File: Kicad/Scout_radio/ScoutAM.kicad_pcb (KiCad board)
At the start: 2 copper layers, 55 x 100 mm, 92 parts, among them J1 Conn_01x07, J2 Conn_01x02, J3 PJ-342, J4 Conn_Coaxial, J5 Conn_01x02, Q1 AO3401A, Q2 2N7002, SW1 B3FS, SW2 B3FS, SW3 B3FS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

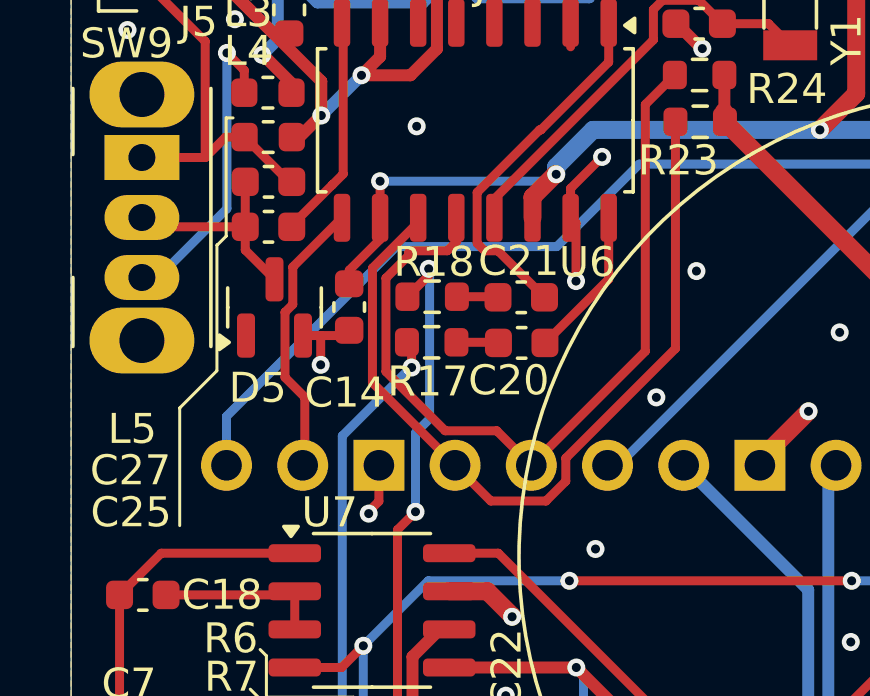
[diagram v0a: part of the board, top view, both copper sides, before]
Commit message: Added software folder
Added software folder with CircuitPython for testing
Fixed hardware cross of SDA and SCL to Si4732
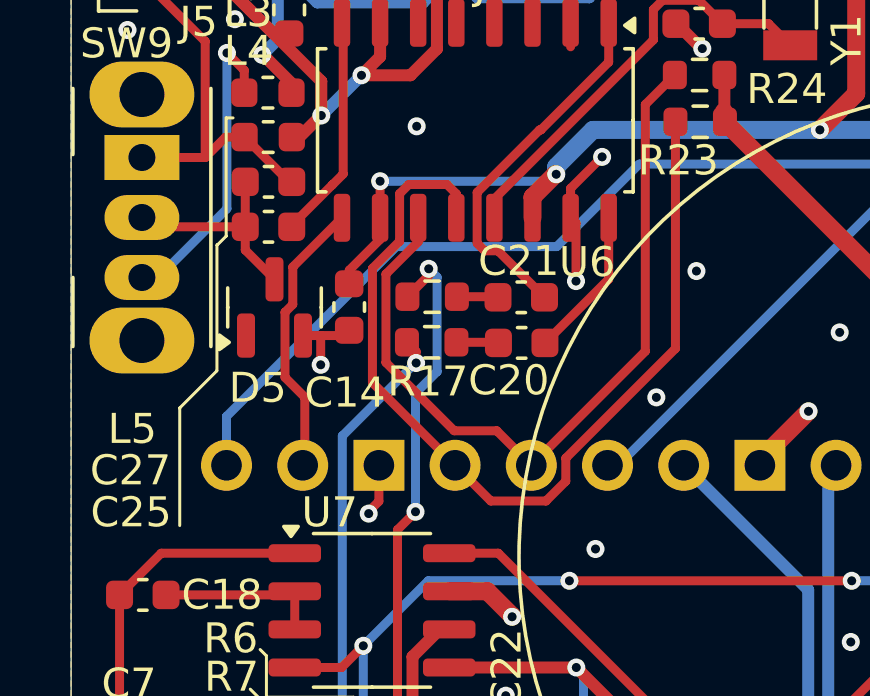
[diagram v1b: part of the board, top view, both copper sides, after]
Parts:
- L4: value 220uh -> 4.7uH
- L5: value 4.7uH -> 220uH
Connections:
- A1 pad 24: /SC -> /SD
- A1 pad 25: /SD -> /SC
- R23 pad 2: /SC -> /SD
- R24 pad 2: /SD -> /SC
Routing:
- net /SD: track 27.9 -> 31.5 mm
- net /SC: track 28.0 -> 26.5 mm
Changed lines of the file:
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@@
 			(layers "F.Cu" "F.Paste" "F.Mask")
 			(roundrect_rratio 0.25)
-			(net 44 "/SD")
+			(net 46 "/SC")
 			(pintype "passive")
 		)
@@
 			)
 		)
-		(property "Value" "220uh"
+		(property "Value" "4.7uH"
 			(at 0 1.43 0)
 			(layer "F.Fab")
@@
 			(layers "F.Cu" "F.Paste" "F.Mask")
 			(roundrect_rratio 0.25)
-			(net 46 "/SC")
+			(net 44 "/SD")
 			(pintype "passive")
 		)
@@
 			)
 		)
-		(property "Value" "4.7uH"
+		(property "Value" "220uH"
 			(at 0 1.43 0)
 			(layer "F.Fab")
@@
 			(at 0.065 -1.16 0)
 			(layer "F.SilkS")
+			(hide yes)
 			(effects
 				(font
@@
 			(layers "*.Cu" "*.Mask")
 			(remove_unused_layers no)
-			(net 46 "/SC")
+			(net 44 "/SD")
 			(pinfunction "GPIO18")
 			(pintype "bidirectional")
@@
 			(layers "*.Cu" "*.Mask")
 			(remove_unused_layers no)
-			(net 44 "/SD")
+			(net 46 "/SC")
 			(pinfunction "GPIO19")
 			(pintype "bidirectional")
@@
 	)
 	(segment
-		(start 81.35 67.36)
-		(end 81.35 66.675)
-		(width 0.3)
-		(layer "F.Cu")
-		(net 24)
-	)
-	(segment
 		(start 75.518604 82.69)
 		(end 78.31 82.69)
@@
 	)
 	(segment
-		(start 81.35 66.675)
-		(end 81.195 66.52)
+		(start 81.500686 66.825686)
+		(end 81.500686 67.209314)
 		(width 0.3)
 		(layer "F.Cu")
@@
 		(net 24)
 	)
+	(segment
+		(start 81.195 66.52)
+		(end 81.500686 66.825686)
+		(width 0.3)
+		(layer "F.Cu")
+		(net 24)
+	)
 	(via
 		(at 79.04 81.96)
@@
 	)
 	(via
-		(at 81.35 67.36)
+		(at 81.500686 67.209314)
 		(size 0.6)
 		(drill 0.3)
@@
 	(segment
 		(start 79.04 69.64)
-		(end 81.32 67.36)
+		(end 81.470686 67.209314)
 		(width 0.3)
 		(layer "B.Cu")
@@
 	)
 	(segment
-		(start 81.32 67.36)
-		(end 81.35 67.36)
+		(start 81.470686 67.209314)
+		(end 81.500686 67.209314)
 		(width 0.3)
 		(layer "B.Cu")
@@
 	)
 	(segment
-		(start 81.95 64.1)
-		(end 81.92 64.07)
+		(start 81.48 72.17)
+		(end 81.48 68.21995)
 		(width 0.3)
 		(layer "B.Cu")
@@
 	)
 	(segment
-		(start 81.48 72.17)
-		(end 81.48 69.54)
+		(start 81.48 68.21995)
+		(end 82.200686 67.499264)
 		(width 0.3)
 		(layer "B.Cu")
@@
 	)
 	(segment
-		(start 81.48 69.54)
-		(end 81.95 69.07)
+		(start 82.200686 64.350686)
+		(end 81.92 64.07)
 		(width 0.3)
 		(layer "B.Cu")
@@
 	)
 	(segment
-		(start 81.95 69.07)
-		(end 81.95 64.1)
+		(start 82.200686 67.499264)
+		(end 82.200686 64.350686)
 		(width 0.3)
 		(layer "B.Cu")
@@
 	)
 	(segment
-		(start 84.19 69.47)
-		(end 82.47005 69.47)
+		(start 80.045 67.865)
+		(end 80.045 64.058603)
 		(width 0.3)
 		(layer "F.Cu")
@@
 	)
 	(segment
-		(start 82.47005 69.47)
-		(end 80.495 67.49495)
+		(start 80.045 64.058603)
+		(end 80.95 63.153603)
 		(width 0.3)
 		(layer "F.Cu")
@@
 	)
 	(segment
-		(start 82.539999 63.47)
-		(end 82.84 63.169999)
+		(start 81.257472 61.26)
+		(end 82.529999 61.26)
 		(width 0.3)
 		(layer "F.Cu")
@@
 	)
 	(segment
-		(start 89.14 66.82)
-		(end 89.14 58.595)
+		(start 82.84 61.570001)
+		(end 82.84 62.37)
 		(width 0.3)
 		(layer "F.Cu")
@@
 	)
 	(segment
-		(start 82.84 63.169999)
-		(end 82.84 62.37)
+		(start 82.8 70.62)
+		(end 80.045 67.865)
 		(width 0.3)
 		(layer "F.Cu")
@@
 	)
 	(segment
-		(start 85.34 70.62)
-		(end 84.19 69.47)
+		(start 90.145 66.728654)
+		(end 86.49 70.383654)
 		(width 0.3)
 		(layer "F.Cu")
@@
 	)
 	(segment
-		(start 81.316396 63.47)
-		(end 82.539999 63.47)
+		(start 85.83 71.81)
+		(end 83.99 71.81)
 		(width 0.3)
 		(layer "F.Cu")
@@
 	)
 	(segment
-		(start 80.495 64.381396)
-		(end 81.25 63.626396)
+		(start 86.49 70.383654)
+		(end 86.49 71.15)
 		(width 0.3)
 		(layer "F.Cu")
@@
 	)
 	(segment
-		(start 81.25 63.536396)
-		(end 81.316396 63.47)
+		(start 80.95 61.567472)
+		(end 81.257472 61.26)
 		(width 0.3)
 		(layer "F.Cu")
@@
 	)
 	(segment
-		(start 80.495 67.49495)
-		(end 80.495 64.381396)
+		(start 80.95 63.153603)
+		(end 80.95 61.567472)
 		(width 0.3)
 		(layer "F.Cu")
@@
 	)
 	(segment
-		(start 81.25 63.626396)
-		(end 81.25 63.536396)
+		(start 86.49 71.15)
+		(end 85.83 71.81)
 		(width 0.3)
 		(layer "F.Cu")
@@
 	)
 	(segment
-		(start 89.14 58.595)
-		(end 90.125 57.61)
+		(start 83.99 71.81)
+		(end 82.8 70.62)
 		(width 0.3)
 		(layer "F.Cu")
@@
 	)
 	(segment
-		(start 85.34 70.62)
-		(end 89.14 66.82)
+		(start 90.145 59.17)
+		(end 90.145 66.728654)
 		(width 0.3)
 		(layer "F.Cu")
@@
 	)
 	(segment
-		(start 81.57 62.522528)
-		(end 81.57 62.37)
+		(start 82.529999 61.26)
+		(end 82.84 61.570001)
 		(width 0.3)
 		(layer "F.Cu")
-		(net 46)
+		(net 44)
 	)
 	(segment
-		(start 90.145 66.728654)
-		(end 86.49 70.383654)
+		(start 84.19 69.47)
+		(end 82.771421 69.47)
 		(width 0.3)
 		(layer "F.Cu")
@@
 	)
 	(segment
-		(start 85.83 71.81)
-		(end 83.99 71.81)
+		(start 80.495 67.193579)
+		(end 80.495 64.244999)
 		(width 0.3)
 		(layer "F.Cu")
@@
 	)
 	(segment
-		(start 80.045 67.865)
-		(end 80.045 64.047528)
+		(start 89.14 66.82)
+		(end 89.14 58.595)
 		(width 0.3)
 		(layer "F.Cu")
@@
 	)
 	(segment
-		(start 86.49 70.383654)
-		(end 86.49 71.15)
+		(start 80.495 64.244999)
+		(end 81.57 63.169999)
 		(width 0.3)
 		(layer "F.Cu")
@@
 	)
 	(segment
-		(start 86.49 71.15)
-		(end 85.83 71.81)
+		(start 82.771421 69.47)
+		(end 80.495 67.193579)
 		(width 0.3)
 		(layer "F.Cu")
@@
 	)
 	(segment
-		(start 80.045 64.047528)
-		(end 81.57 62.522528)
+		(start 81.57 63.169999)
+		(end 81.57 62.37)
 		(width 0.3)
 		(layer "F.Cu")
@@
 	)
 	(segment
-		(start 82.8 70.62)
-		(end 80.045 67.865)
+		(start 85.34 70.62)
+		(end 84.19 69.47)
 		(width 0.3)
 		(layer "F.Cu")
@@
 	)
 	(segment
-		(start 83.99 71.81)
-		(end 82.8 70.62)
+		(start 89.14 58.595)
+		(end 90.125 57.61)
 		(width 0.3)
 		(layer "F.Cu")
@@
 	)
 	(segment
-		(start 90.145 59.17)
-		(end 90.145 66.728654)
+		(start 85.34 70.62)
+		(end 89.14 66.82)
 		(width 0.3)
 		(layer "F.Cu")

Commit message: Recent changes
Sorry lost track of the changes. So created a new branch!
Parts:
- added R25: 10k, Resistor_SMD:R_0603_1608Metric, F.Cu at (59.0, 74.2)
- added R26: 10k, Resistor_SMD:R_0603_1608Metric, F.Cu at (71.9, 73.6)
- D1: value LED_Red -> LED_Blue
- R8: value 1k -> 2k
- U4: value LISM303 -> GY511; footprint Scout:LISM303 -> Scout:GY511
- moved U4 3.61 mm to (93.6, 97.5)
- moved C18 1.58 mm to (71.9, 76.4)
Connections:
- Q1 pad 1: VSYS -> +5V
- Q1 pad 2: VSYS -> Net-(Q1-S)
- SW8 pad 2: VSYS -> Net-(Q1-S)
- U4 pad 1: GND -> +3.3V
- U4 pad 2: /SDA -> unconnected-(U4-3.3V-Pad2)
- U4 pad 3: /SCL -> GND
- U4 pad 4: +3.3V -> /SCL
- U4 pad 5: unconnected-(U4-RDY-Pad5) -> /SDA
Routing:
- net /ENC_B: track 34.8 -> 0.00 mm
- net Net-(Q1-S): track 0.00 -> 33.5 mm
- net VSYS: track 33.4 -> 0.00 mm
- net /ENC_A: track 40.0 -> 9.02 mm, vias 1 -> 0
- net /ENC_SW: track 34.4 -> 16.5 mm
- net /LAMP: track 57.4 -> 40.1 mm
- net +3.3V: track 91.0 -> 79.0 mm
- net GND: track 300.7 -> 293.2 mm
- net /SDA: track 20.3 -> 14.7 mm
- net /TORCH: track 40.4 -> 44.3 mm
- net /SCL: track 21.3 -> 19.1 mm
- net Net-(U7-BYP): track 5.61 -> 6.37 mm
